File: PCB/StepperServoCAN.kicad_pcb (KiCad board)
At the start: 2 copper layers, 56 x 43.2 mm, 132 parts, among them J1 Debug, J2 CAR, J3 Motor, J4 Conn_01x02, Q1 BSS84, SW1 Rst, SW2 Fcn>, SW3 Fcn>, U1 XL1509-adj, U2 STM32F103CBT6, U3 LMV321, U4 A4950E, U5 A4950E, U6 LMV321, U7 TLE5012B, U8 SN65HVD230, Y1 16Mhz 9pF

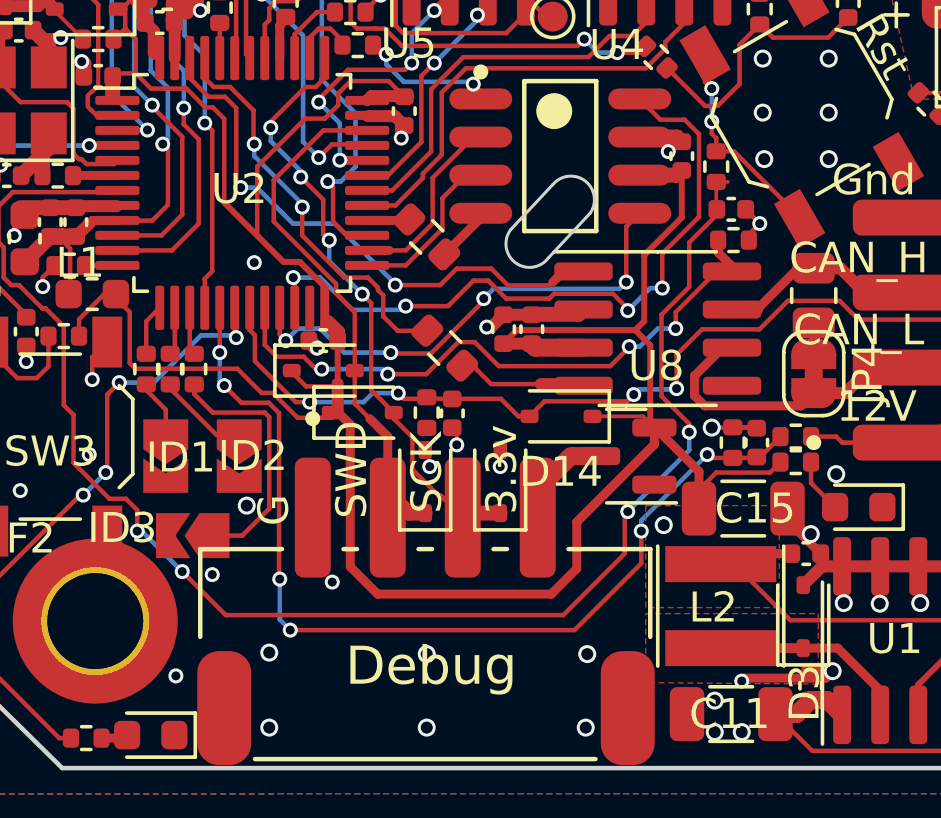
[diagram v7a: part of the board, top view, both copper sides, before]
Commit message: Added VBATT_ADC protection agains large negative and positive voltages
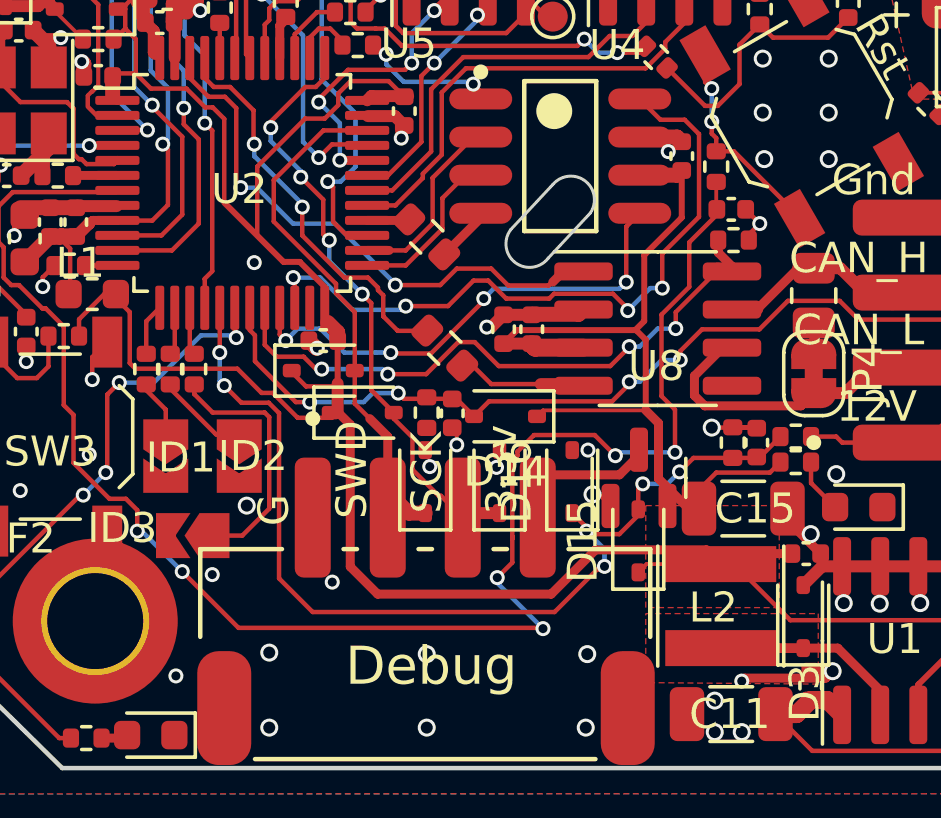
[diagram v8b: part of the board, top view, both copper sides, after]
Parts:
- added D15: 1N5819WS, Diode_SMD:D_SOD-323, F.Cu at (102.6, 112.8)
- added D16: 1N5819WS, Diode_SMD:D_SOD-323, F.Cu at (100.4, 110.8)
- moved D14 1.85 mm to (98.2, 108.7)
- moved Q1 0.84 mm to (102.6, 110.7), turned to 90 degrees
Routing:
- net Net-(U2-NRST): track 50.5 -> 55.2 mm, vias 4 -> 6
- net +3.3V: track 108.4 -> 112.5 mm
- net /+3.3_Ext: track 2.38 -> 4.03 mm
- net GND: track 62.5 -> 63.3 mm, vias 152 -> 153
- net VBATT_ADC: track 32.2 -> 32.8 mm
